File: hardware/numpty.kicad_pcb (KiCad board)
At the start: 2 copper layers, 80 x 127.5 mm, 64 parts, among them J1 usb-c_2.0, J2 AVR-ISP, U1 ATmega32U4-AU, U2 MP3202, Y1 16MHz

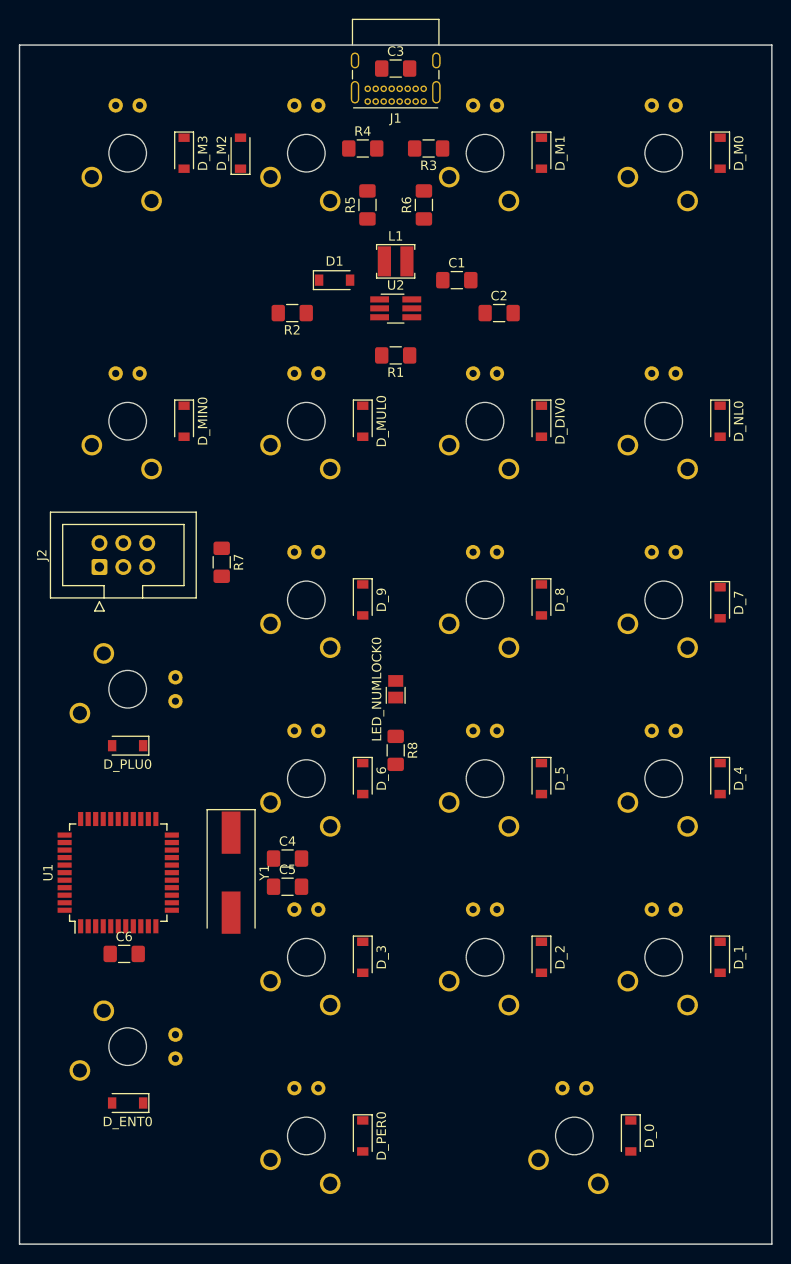
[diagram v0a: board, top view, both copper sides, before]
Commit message: Run traces and fills.
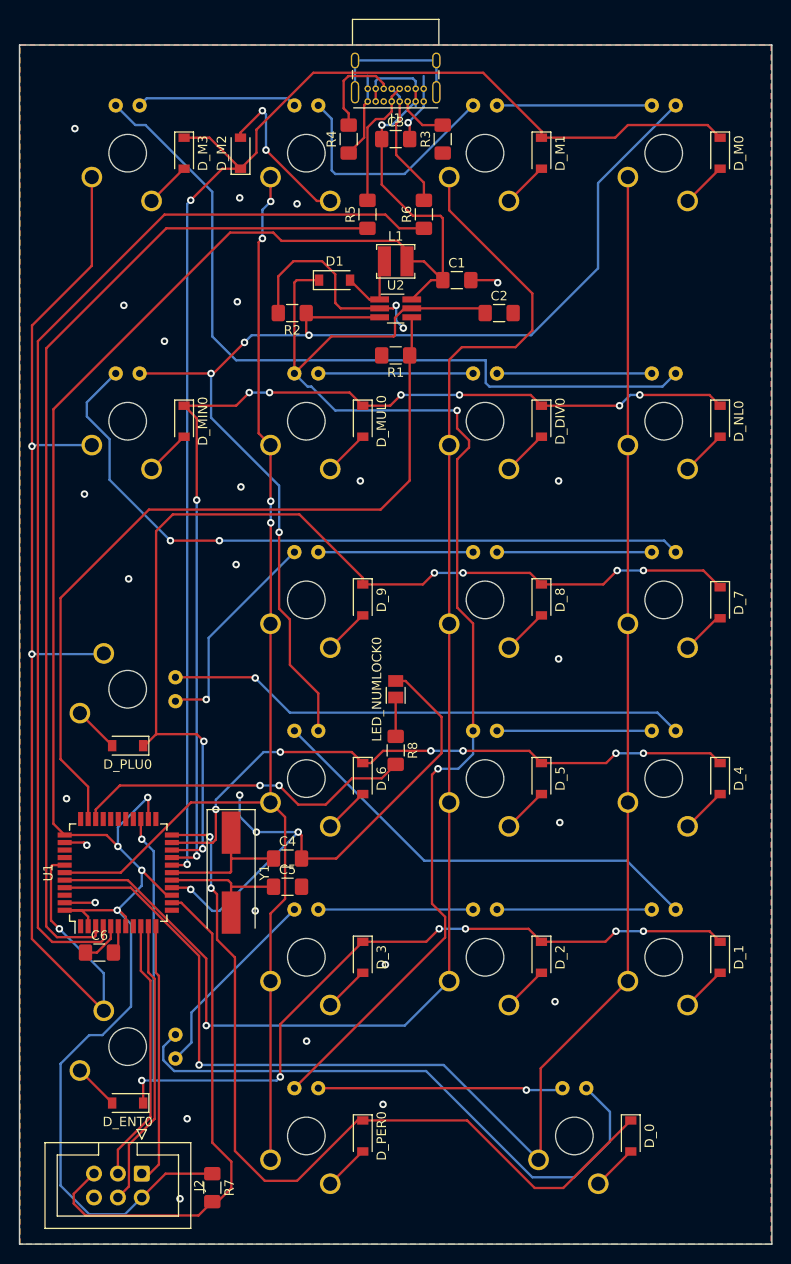
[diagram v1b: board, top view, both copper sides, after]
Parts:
- moved R7 66.5 mm to (-48.0, 81.5)
- moved J2 64.7 mm to (-55.5, 80.0), turned to 270 degrees
- moved C3 7.50 mm to (-28.5, -30.0)
- moved C6 2.64 mm to (-60.0, 56.5)
- moved R3 1.80 mm to (-23.5, -30.0), turned to 90 degrees
- moved R4 1.80 mm to (-33.5, -30.0), turned to 90 degrees
- moved R5 1.00 mm to (-31.5, -22.0)
- moved R6 1.00 mm to (-25.5, -22.0)
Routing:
- net +5V: track 0.00 -> 229.5 mm, vias 0 -> 5
- net COL0: track 0.00 -> 177.6 mm, vias 0 -> 1
- net COL1: track 0.00 -> 149.6 mm, vias 0 -> 1
- net ROW0: track 0.00 -> 147.5 mm, vias 0 -> 2
- net LEDS_ANODE: track 0.00 -> 139.9 mm, vias 0 -> 2
- net COL2: track 0.00 -> 131.9 mm, vias 0 -> 4
- net COL3: track 0.00 -> 127.7 mm, vias 0 -> 3
- net LEDS_CATHODE: track 0.00 -> 127.3 mm, vias 0 -> 4
- net D+: track 0.00 -> 118.7 mm
- net GND: track 0.00 -> 113.6 mm, vias 0 -> 32
- net ROW1: track 0.00 -> 111.2 mm, vias 0 -> 8
- net ROW2: track 0.00 -> 110.2 mm, vias 0 -> 6
- net D-: track 0.00 -> 107.7 mm
- net ROW4: track 0.00 -> 103.8 mm, vias 0 -> 7
- net ROW5: track 0.00 -> 90.7 mm, vias 0 -> 2
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- added copper zone on B.Cu, net GND
- added copper zone on F.Cu, net GND
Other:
- net class Default: clearance 0.2 -> 0.1
- rule trace_clearance: 0.2 -> 0.1

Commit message: Started tidy up (silk screen etc).
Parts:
- NUM LOCK: renamed from SW_NL0
- U1: value ATmega32U4-AU -> ATmega32U4
- renumbered SW_MUL0 to *, SW_PLU0 to +, SW_MIN0 to -, SW_PER0 to ., SW_DIV0 to /, SW_0 to 0, SW_1 to 1, SW_2 to 2, SW_3 to 3, SW_4 to 4, SW_5 to 5, SW_6 to 6, SW_7 to 7, SW_8 to 8, SW_9 to 9, SW_ENT0 to ENTER, SW_M0 to M0, SW_M1 to M1, SW_M2 to M2, SW_M3 to M3

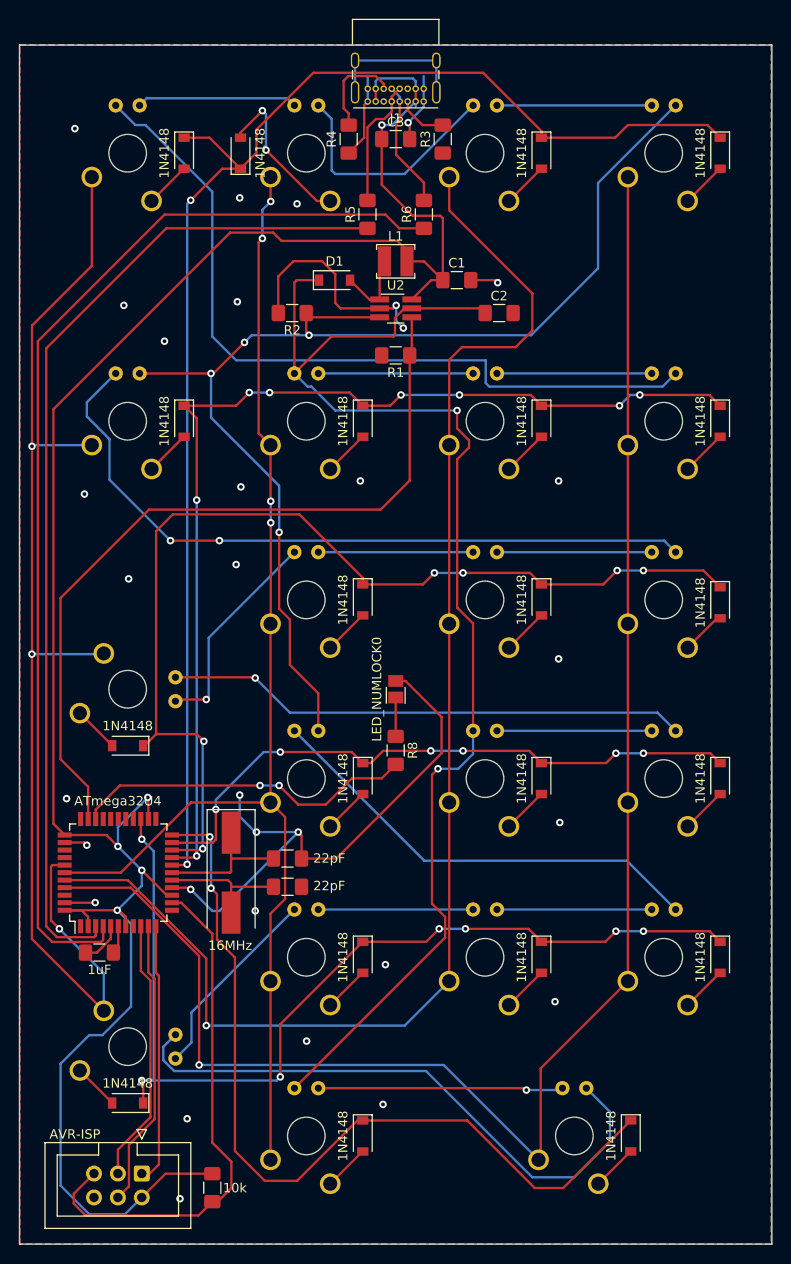
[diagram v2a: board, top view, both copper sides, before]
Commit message: Moved led pins to port B.  Added push-button on port B.  Reworked layout to suit these changes.
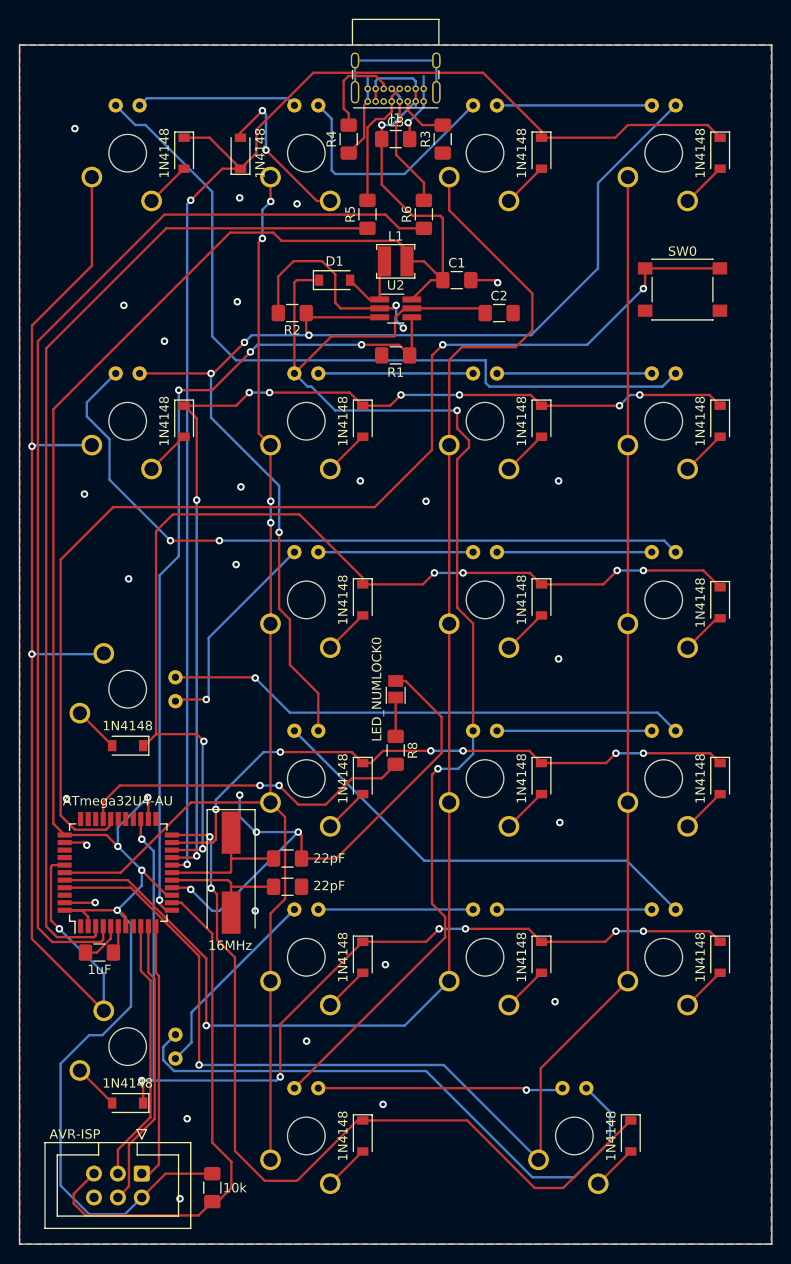
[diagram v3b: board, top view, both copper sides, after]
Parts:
- added SW0: SW_Push, Button_Switch_SMD:SW_Push_1P1T_NO_6x6mm_H9.5mm, F.Cu at (2.00, -14.0)
- SW_NL0: renamed from NUM LOCK
- U1: value ATmega32U4 -> ATmega32U4-AU
- renumbered 0 to SW_0, 1 to SW_1, 2 to SW_2, 3 to SW_3, 4 to SW_4, 5 to SW_5, 6 to SW_6, 7 to SW_7, 8 to SW_8, 9 to SW_9, / to SW_DIV0, ENTER to SW_ENT0, M0 to SW_M0, M1 to SW_M1, M2 to SW_M2, M3 to SW_M3, - to SW_MIN0, * to SW_MUL0, . to SW_PER0, + to SW_PLU0
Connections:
- U1 pad 12: Net-(U1-Pad12) -> LEDS_PWM
- U1 pad 30: Net-(U1-Pad30) -> Net-(R8-Pad2)
- U1 pad 31: Net-(R8-Pad2) -> Net-(U1-Pad31)
- U1 pad 32: LEDS_PWM -> Net-(U1-Pad32)
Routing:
- net Net-(SW0-Pad1): track 0.00 -> 123.9 mm, vias 0 -> 2
- net LEDS_PWM: track 84.5 -> 88.2 mm, vias 0 -> 4
- net GND: vias 32 -> 33

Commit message: Cleaned up rev 0 PCB layout, ordered fabrication.  Added .gitignore.
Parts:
- added G***: LOGO, numpty:osha_logo_8mm, F.Cu at (-57.0, 17.0)
- added G***: LOGO, numpty:clewsy_logo_8mm, F.Cu at (-57.0, -14.0)
- added G***: LOGO, numpty:clewsy_logo_8mm, B.Cu at (-28.5, -14.5)
- added G***: LOGO, numpty:osha_logo_8mm, B.Cu at (5.00, 77.0)
- D1: value 30V_500mA_Schottky -> Schottky
- J1: value usb-c_2.0 -> usb-c
- R8: value 300 -> 100
- renumbered SW_MUL0 to *, SW_PLU0 to +, SW_MIN0 to -, SW_PER0 to ., SW_DIV0 to /, SW_0 to 0, SW_1 to 1, SW_2 to 2, SW_3 to 3, SW_4 to 4, SW_5 to 5, SW_6 to 6, SW_7 to 7, SW_8 to 8, SW_9 to 9, SW_ENT0 to ENTER, SW_M0 to M0, SW_M1 to M1, SW_M2 to M2, SW_M3 to M3, SW_NL0 to NUMLOCK
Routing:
- net +5V: track 229.5 -> 228.3 mm
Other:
- board text added: "clews.pro"
